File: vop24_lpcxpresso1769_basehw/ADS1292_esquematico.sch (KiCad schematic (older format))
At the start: 10 parts

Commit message: Esquematico:    - terminar conexiones de ads: revisar slau387.pdf para conexiones de caps y bobinas    - ver slau387.pdf para medicion de fuente y conexion usb
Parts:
- removed C? (x4): C_Small, symbol C_Small
- removed C?: 4.7nF, symbol C_Small
- added 100k, 10k, 10k? (x2), 1M: R_Small, symbol R_Small
- added C?: 4.7nF, symbol C_Small
- added C?: 1uF, symbol C_Small
- added C?: 1.5nF, symbol C_Small
- added J? (x3): Conn_01x02, symbol Conn_01x02
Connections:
- net labels added: CLK, CLKSEL, GNDA, GNDD, GPIO1, GPIO2, RLDIN, RLDINV, RLDOUT, SENS3N, SENS3P, START_ADS, VCAP2, ~CS~_ADS, ~PWDNE~_ADS
- net labels removed: CS_ADS
- wire segments 42 -> 80
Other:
- note added: "Conexión directa a las \nentradas del ADS. Tener\n en cuenta que la entrada\n 3 esta multiplexada a \nalguno de los otros \n2 adcs\n"
- note added: "agregar filtros analogicos"

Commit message: Esquematico ADS1292:    - invertir valor y nombre de todas las resistencias (puse el valor en el campo nombre :( )    - agregar protecciones y desacoples como en la nota de aplicacion    - terminar filtros analogicos
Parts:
- added 1M, 1M?, 33k, 33k?: R_Small, symbol R_Small
- added C? (x3): 470pF, symbol C_Small
- added J?: Conn_01x02, symbol Conn_01x02
- R?: renamed from 1M; value R_Small -> 1M
- R?: renamed from 100k; value R_Small -> 100k
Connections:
- wire segments 80 -> 108
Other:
- note added: "FILTRO ANALOGICO ENTRADA 1\n"
- note removed: "agregar filtros analogicos"

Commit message: Esquematico ADS:    - version a revisar. Falta agregar medicion de bateria y carga USB como en la nota de aplicacion
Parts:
- removed 10k?, 1M?, 33k?: R_Small, symbol R_Small
- added C? (x6): 470pF, symbol C_Small
- added C? (x2): 1uF, symbol C_Small
- added C? (x2): 0.1uF, symbol C_Small
- added FB?: BLM18PG121SN1D, digikey-footprints:0603, symbol BLM18PG121SN1D
- added J? (x2): Conn_01x02, symbol Conn_01x02
- added R?: 10k, symbol R_Small
- added R? (x5): 33k, symbol R_Small
- added R? (x5): 1M, symbol R_Small
- R?: renamed from 10k; value R_Small -> 10k
- R?: renamed from 10k?; value R_Small -> 10k
- R?: renamed from 1M; value R_Small -> 1M
- R?: renamed from 33k; value R_Small -> 33k
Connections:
- wire segments 108 -> 165
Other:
- note added: "Desacople de la alimentacion\ndel ADS1292. Poner los caps\ncerca de los pines de alimentacion\n"
- note added: "FILTRO ANALOGICO ENTRADA 2"
- note added: "FILTRO ANALOGICO ENTRADA 3"

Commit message: Esquematico Comunicacion: falta agregar USB, BLE y UART
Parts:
- C? (x20): symbol C_Small -> Device:C_Small
- FB?: symbol BLM18PG121SN1D -> vop24_lpcxpresso1769_basehw-rescue:BLM18PG121SN1D
- J? (x6): symbol Conn_01x02 -> Connector_Generic:Conn_01x02
- R? (x17): symbol R_Small -> Device:R_Small
- U?: symbol ADS1292 -> vop24_lpcxpresso1769_basehw-rescue:ADS1292

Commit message: Primera versión esquematico sin revisar
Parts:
- removed J? (x3): Conn_01x02, symbol Connector_Generic:Conn_01x02
- added J5, J6, J7: Conn_01x04, symbol Connector_Generic:Conn_01x04
- added R11, R12, R13: 33k, symbol Device:R_Small
- added U5, U6, U7: LM334, symbol vop24_lpcxpresso1769_basehw-rescue:LM334
- gave numbers to parts that had none: 42
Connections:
- net labels removed: GNDD
- wire segments 165 -> 198
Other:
- moved on the sheet: C12, C13, C14, C15, C16, C17, C18, C19, C20, R14, R15, R16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

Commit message: Algunas correcciones sobre el esquemático. Falta terminar de revisar algunos conflictos del DRC
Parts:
- renumbered C1 to C401, C2 to C402, C3 to C403, C4 to C404, C5 to C405, C6 to C406, C7 to C407, C8 to C408, C9 to C409, C10 to C410, C11 to C411, C12 to C412, C13 to C413, C14 to C414, C15 to C415, C16 to C416, C17 to C417, C18 to C418, C19 to C419, C20 to C420, FB1 to FB401, J2 to J401, J3 to J402, J4 to J403, J5 to J404, J6 to J405, J7 to J406, R6 to R401, R7 to R402, R8 to R403, R9 to R404, R10 to R405, R11 to R406, R12 to R407, R13 to R408, R14 to R409, R15 to R410, R16 to R411, R17 to R412, R18 to R413, R19 to R414, R20 to R415, R21 to R416, R22 to R417, R23 to R418, R24 to R419, R25 to R420, U4 to U401, U5 to U402, U6 to U403, U7 to U404

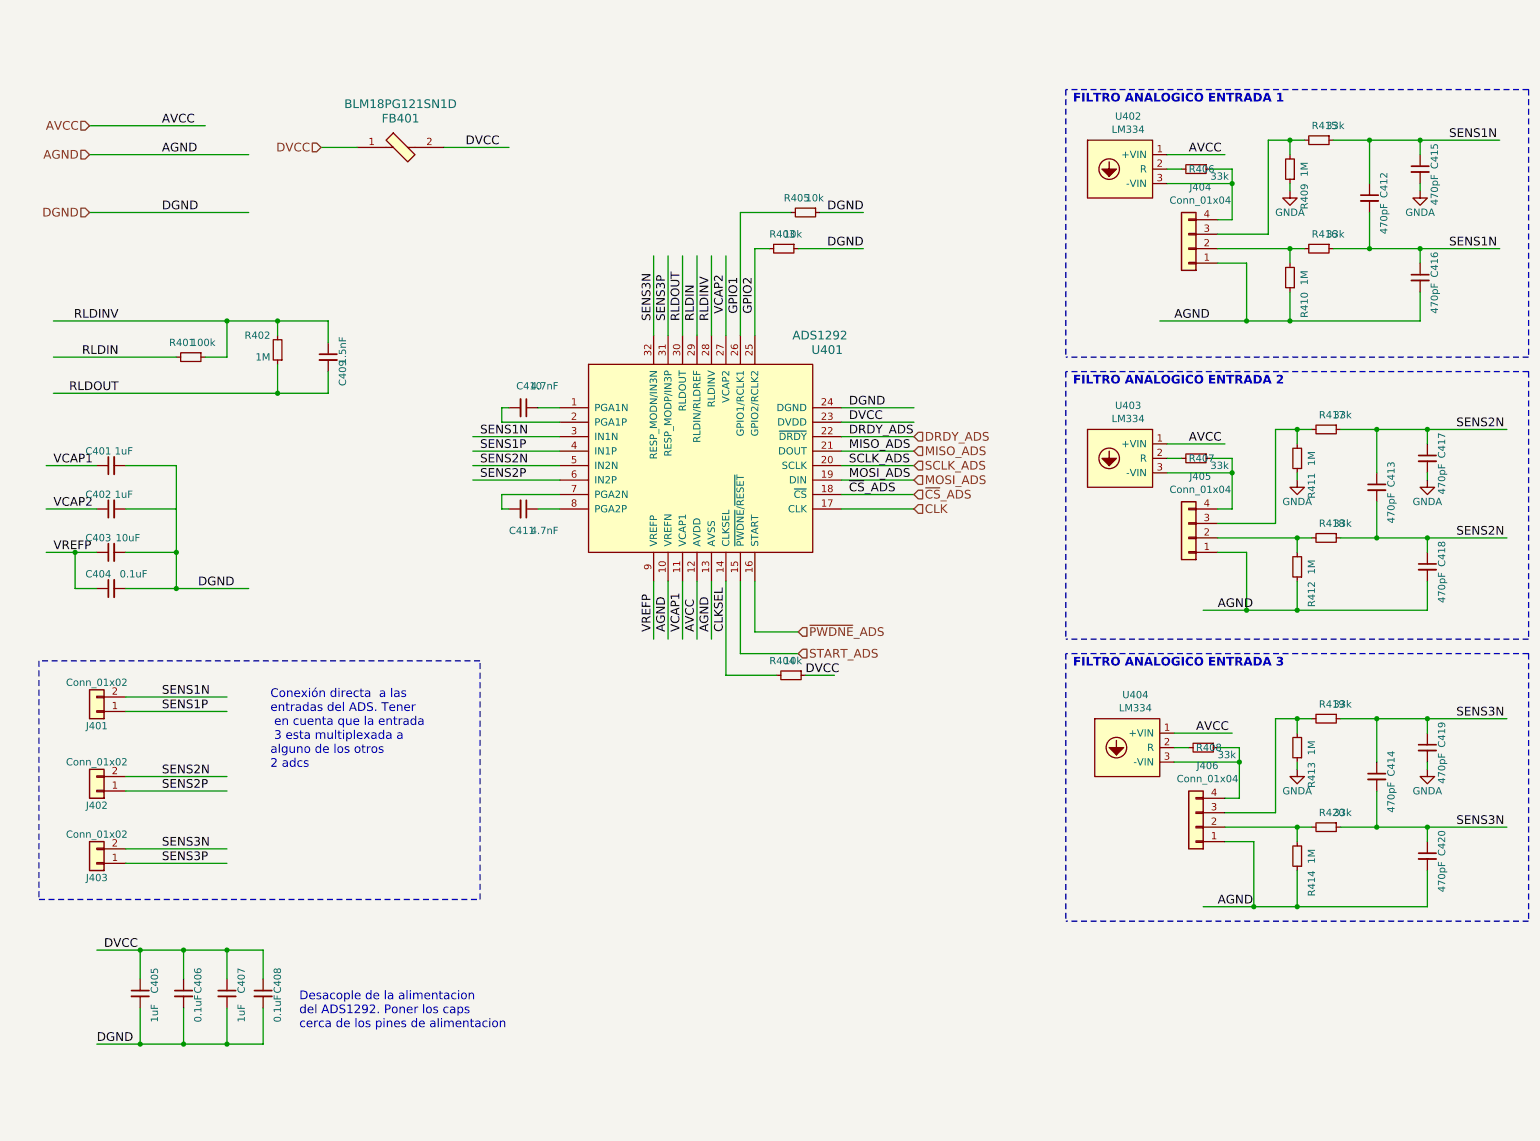
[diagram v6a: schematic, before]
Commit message: Correcciones de esquemático:    - resueltos todos los conflictos de DRC    - cambio de circutio de medicion de temp    - ordenados todas las etiquetas y valores
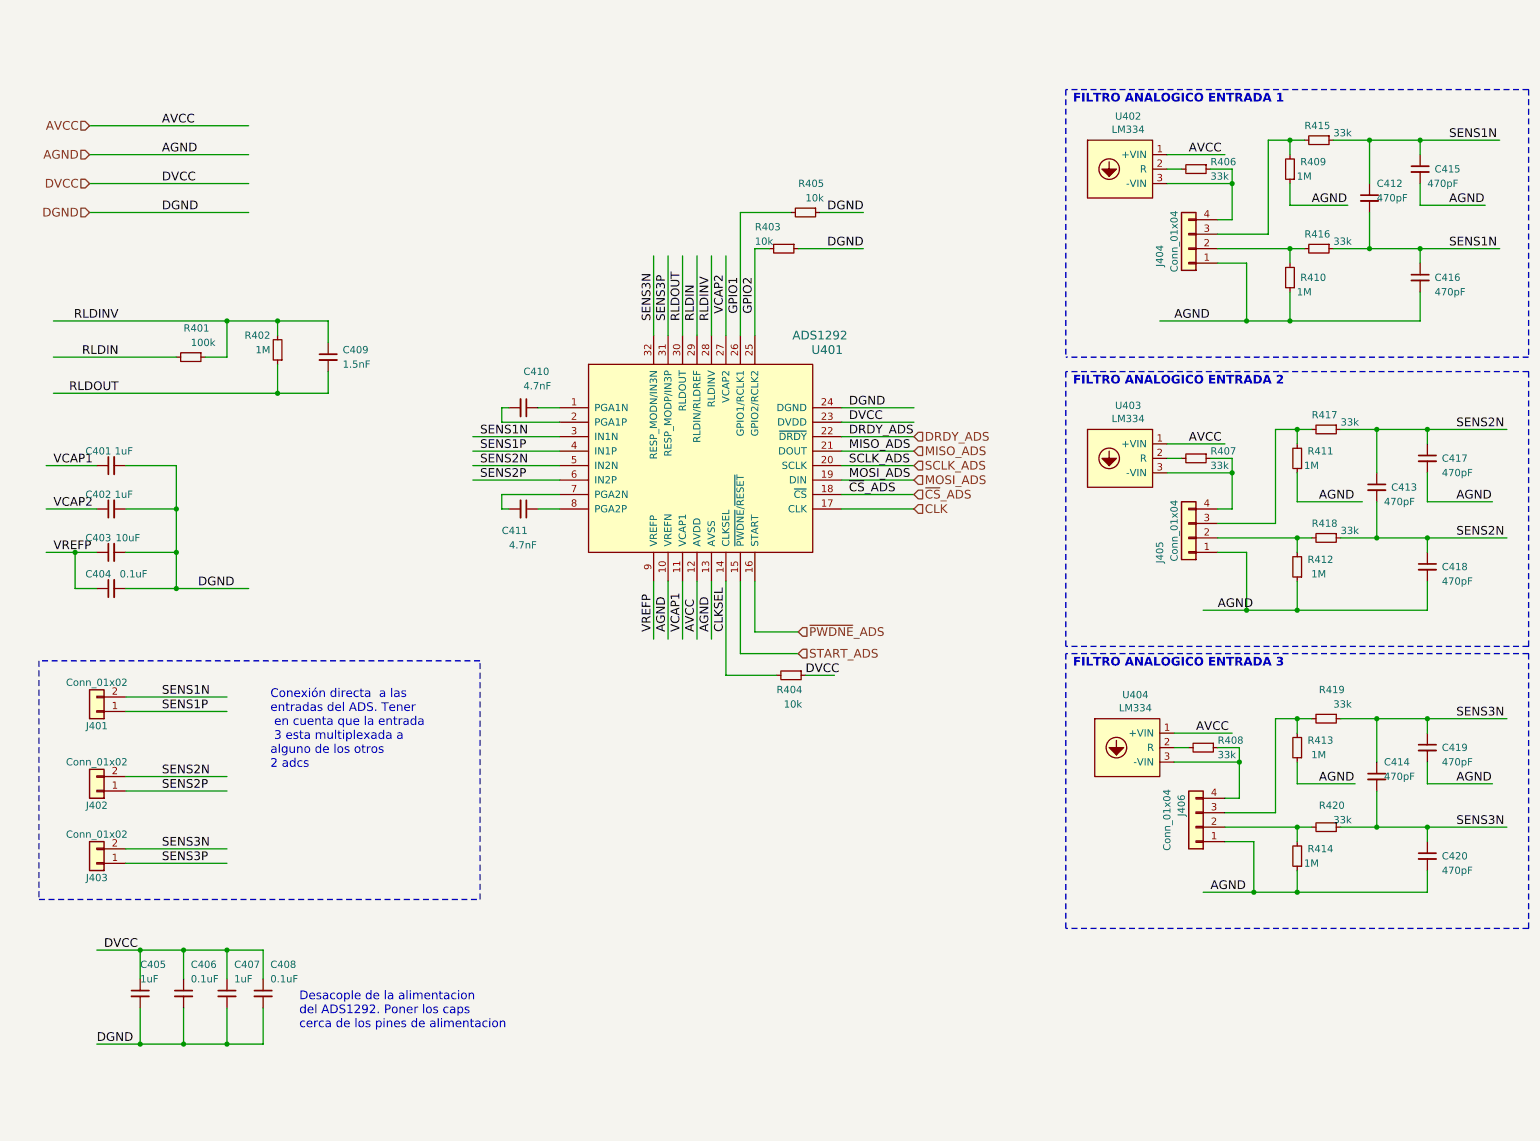
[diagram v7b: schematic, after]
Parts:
- removed FB401: BLM18PG121SN1D, digikey-footprints:0603, symbol vop24_lpcxpresso1769_basehw-rescue:BLM18PG121SN1D
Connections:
- net labels removed: GNDA
- wire segments 198 -> 204

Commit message: Se agregaron la mayoría de los footprints de los ICs
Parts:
- U401: footprint (none) -> meport_kicad_libs:PQFP-G32_7x7mm_P0.5mm
- U402, U403, U404: footprint (none) -> Package_TO_SOT_THT:TO-92_Inline_Wide
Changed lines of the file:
@@
 F 0 "U401" H 6100 3850 60  0000 C CNN
 F 1 "ADS1292" H 6050 3950 60  0000 C CNN
-F 2 "" H 5150 2750 60  0001 C CNN
+F 2 "meport_kicad_libs:PQFP-G32_7x7mm_P0.5mm" H 5150 2750 60  0001 C CNN
 F 3 "" H 5150 2750 60  0001 C CNN
 	1    5250 3100
@@
 F 0 "U402" H 8181 1565 50  0000 C CNN
 F 1 "LM334" H 8181 1474 50  0000 C CNN
-F 2 "" H 8050 1200 50  0001 C CNN
+F 2 "Package_TO_SOT_THT:TO-92_Inline_Wide" H 8050 1200 50  0001 C CNN
 F 3 "" H 8050 1200 50  0001 C CNN
 	1    8150 1150
@@
 F 0 "U403" H 8181 3565 50  0000 C CNN
 F 1 "LM334" H 8181 3474 50  0000 C CNN
-F 2 "" H 8050 3200 50  0001 C CNN
+F 2 "Package_TO_SOT_THT:TO-92_Inline_Wide" H 8050 3200 50  0001 C CNN
 F 3 "" H 8050 3200 50  0001 C CNN
 	1    8150 3150
@@
 F 0 "U404" H 8231 5565 50  0000 C CNN
 F 1 "LM334" H 8231 5474 50  0000 C CNN
-F 2 "" H 8100 5200 50  0001 C CNN
+F 2 "Package_TO_SOT_THT:TO-92_Inline_Wide" H 8100 5200 50  0001 C CNN
 F 3 "" H 8100 5200 50  0001 C CNN
 	1    8200 5150
